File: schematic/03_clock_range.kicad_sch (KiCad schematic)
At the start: 23 parts, among them SW113 start / stop, SW114 octaves: stop at 3, U101 TLC555IDR, U102 TLC555IDR, U403 74HC14

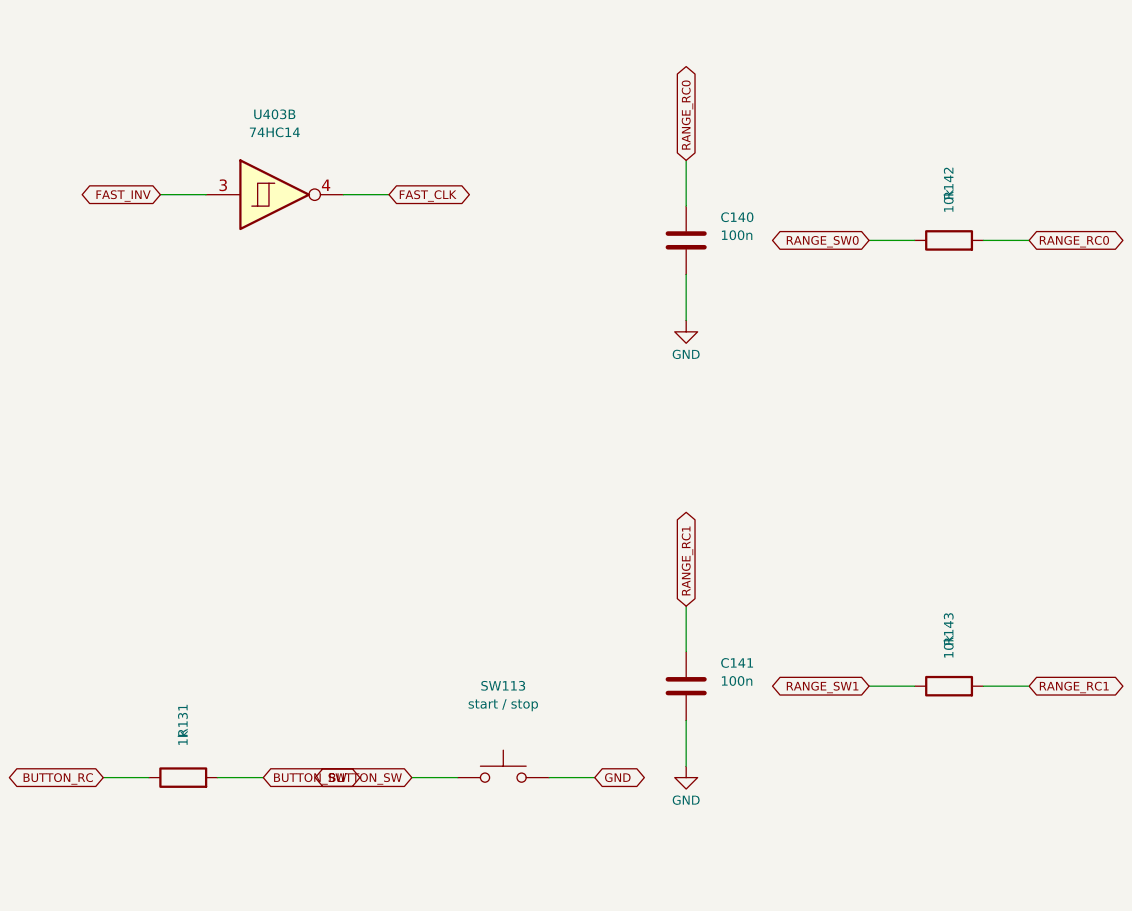
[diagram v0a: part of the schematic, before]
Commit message: add the pitch and sound circuit
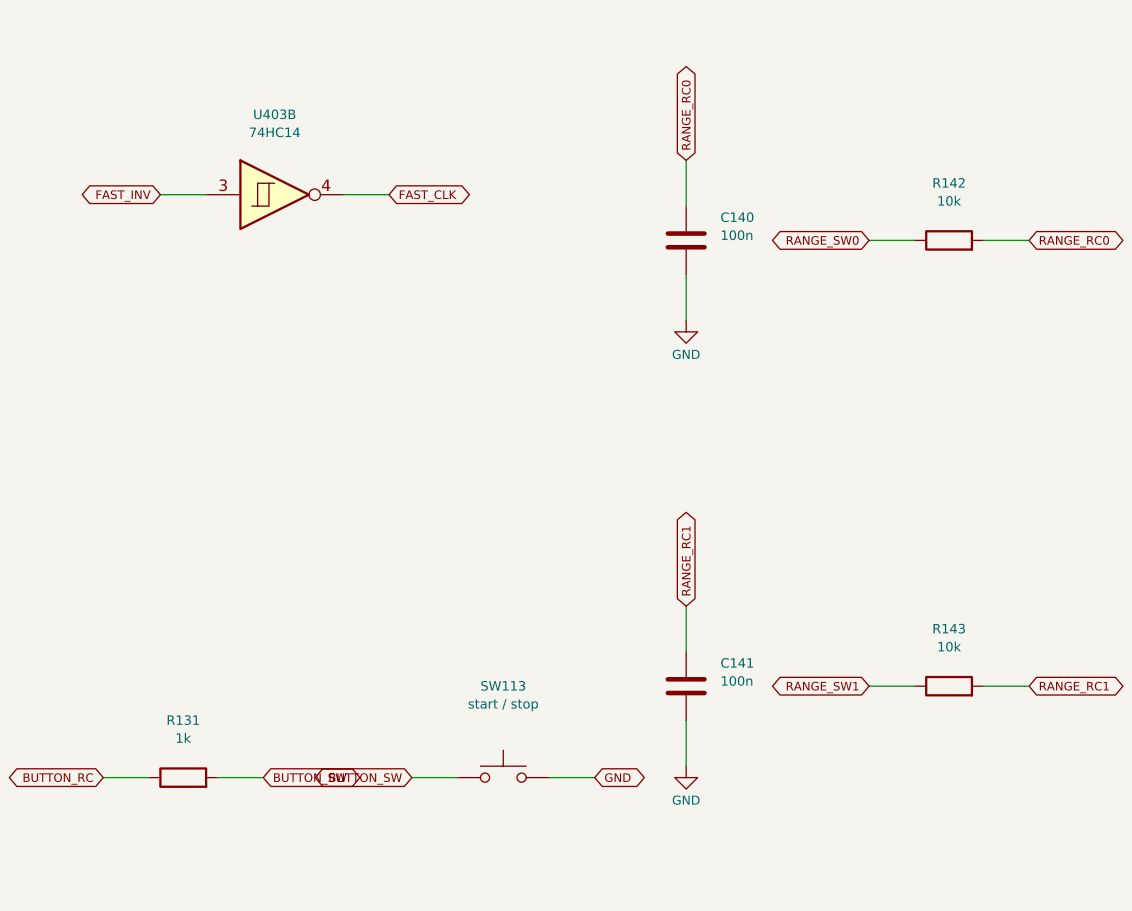
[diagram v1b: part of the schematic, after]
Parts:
- C181: footprint Capacitor_SMD:C_0805_2012Metric -> (none)
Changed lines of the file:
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@@
       )
     )
-    (property "Footprint" "Capacitor_SMD:C_0805_2012Metric"
+    (property "Footprint" ""
       (at 308.61 97.78999999999999 0.0)
       (effects
@@
     (dnp no)
     (property "Reference" "R131"
-      (at 119.38 223.52 0.0)
+      (at 119.38 223.52 90.0)
       (effects
         (font
@@
     )
     (property "Value" "1k"
-      (at 119.38 225.52 0.0)
+      (at 119.38 225.52 90.0)
       (effects
         (font
@@
     )
     (property "Footprint" "Resistor_SMD:R_0805_2012Metric"
-      (at 119.38 223.52 0.0)
+      (at 119.38 223.52 90.0)
       (effects
         (font
@@
     )
     (property "Datasheet" ""
-      (at 119.38 223.52 0.0)
+      (at 119.38 223.52 90.0)
       (effects
         (font
@@
     (dnp no)
     (property "Reference" "R142"
-      (at 204.47 163.83 0.0)
+      (at 204.47 163.83 90.0)
       (effects
         (font
@@
     )
     (property "Value" "10k"
-      (at 204.47 165.83 0.0)
+      (at 204.47 165.83 90.0)
       (effects
         (font
@@
     )
     (property "Footprint" "Resistor_SMD:R_0805_2012Metric"
-      (at 204.47 163.83 0.0)
+      (at 204.47 163.83 90.0)
       (effects
         (font
@@
     )
     (property "Datasheet" ""
-      (at 204.47 163.83 0.0)
+      (at 204.47 163.83 90.0)
       (effects
         (font
@@
     (dnp no)
     (property "Reference" "R143"
-      (at 204.47 213.36 0.0)
+      (at 204.47 213.36 90.0)
       (effects
         (font
@@
     )
     (property "Value" "10k"
-      (at 204.47 215.36 0.0)
+      (at 204.47 215.36 90.0)
       (effects
         (font
@@
     )
     (property "Footprint" "Resistor_SMD:R_0805_2012Metric"
-      (at 204.47 213.36 0.0)
+      (at 204.47 213.36 90.0)
       (effects
         (font
@@
     )
     (property "Datasheet" ""
-      (at 204.47 213.36 0.0)
-      (effects
-        (font
+      (at 204.47 213.36 90.0)
+      (effects
+        (font

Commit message: add power supply, rail checks and parts list
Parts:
- U101, U102: MPN (none) -> TLC555IDR; Manufacturer (none) -> Texas Instruments; Supplier (none) -> LCSC
- U403: MPN (none) -> 74HC14D,653; Manufacturer (none) -> Nexperia; Supplier (none) -> LCSC
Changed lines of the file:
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@@
       )
     )
-    (property "Datasheet" "http://www.ti.com/lit/ds/symlink/tlc555.pdf"
+    (property "Datasheet" "https://www.ti.com/lit/ds/symlink/tlc555.pdf"
       (at 62.230000000000004 57.15000000000001 0.0)
       (effects
@@
       )
     )
+    (property "MPN" "TLC555IDR"
+      (at 80.01 74.93 0.0)
+      (effects
+        (font
+          (size 1.0 1.0)
+        )
+        (hide yes)
+      )
+    )
+    (property "Manufacturer" "Texas Instruments"
+      (at 80.01 74.93 0.0)
+      (effects
+        (font
+          (size 1.0 1.0)
+        )
+        (hide yes)
+      )
+    )
+    (property "Supplier" "LCSC"
+      (at 80.01 74.93 0.0)
+      (effects
+        (font
+          (size 1.0 1.0)
+        )
+        (hide yes)
+      )
+    )
     (instances
       (project "arpeggiator"
@@
       )
     )
-    (property "Datasheet" "http://www.ti.com/lit/ds/symlink/tlc555.pdf"
+    (property "Datasheet" "https://www.ti.com/lit/ds/symlink/tlc555.pdf"
       (at 247.65 57.15000000000001 0.0)
       (effects
@@
       )
     )
+    (property "MPN" "TLC555IDR"
+      (at 265.43 74.93 0.0)
+      (effects
+        (font
+          (size 1.0 1.0)
+        )
+        (hide yes)
+      )
+    )
+    (property "Manufacturer" "Texas Instruments"
+      (at 265.43 74.93 0.0)
+      (effects
+        (font
+          (size 1.0 1.0)
+        )
+        (hide yes)
+      )
+    )
+    (property "Supplier" "LCSC"
+      (at 265.43 74.93 0.0)
+      (effects
+        (font
+          (size 1.0 1.0)
+        )
+        (hide yes)
+      )
+    )
     (instances
       (project "arpeggiator"
@@
       )
     )
-    (property "Datasheet" "http://www.ti.com/lit/gpn/sn74HC14"
+    (property "Datasheet" "https://assets.nexperia.com/documents/data-sheet/74HC_HCT14.pdf"
       (at 69.85 156.20999999999998 0.0)
       (effects
@@
       )
     )
+    (property "MPN" "74HC14D,653"
+      (at 69.85 165.1 0.0)
+      (effects
+        (font
+          (size 1.0 1.0)
+        )
+        (hide yes)
+      )
+    )
+    (property "Manufacturer" "Nexperia"
+      (at 69.85 165.1 0.0)
+      (effects
+        (font
+          (size 1.0 1.0)
+        )
+        (hide yes)
+      )
+    )
+    (property "Supplier" "LCSC"
+      (at 69.85 165.1 0.0)
+      (effects
+        (font
+          (size 1.0 1.0)
+        )
+        (hide yes)
+      )
+    )
     (instances
       (project "arpeggiator"
@@
       )
     )
-    (property "Datasheet" "http://www.ti.com/lit/gpn/sn74HC14"
+    (property "Datasheet" "https://assets.nexperia.com/documents/data-sheet/74HC_HCT14.pdf"
       (at 129.54 156.20999999999998 0.0)
       (effects
@@
       )
     )
+    (property "MPN" "74HC14D,653"
+      (at 129.54 165.1 0.0)
+      (effects
+        (font
+          (size 1.0 1.0)
+        )
+        (hide yes)
+      )
+    )
+    (property "Manufacturer" "Nexperia"
+      (at 129.54 165.1 0.0)
+      (effects
+        (font
+          (size 1.0 1.0)
+        )
+        (hide yes)
+      )
+    )
+    (property "Supplier" "LCSC"
+      (at 129.54 165.1 0.0)
+      (effects
+        (font
+          (size 1.0 1.0)
+        )
+        (hide yes)
+      )
+    )
     (instances
       (project "arpeggiator"
@@
       )
     )
-    (property "Datasheet" "http://www.ti.com/lit/gpn/sn74HC14"
+    (property "Datasheet" "https://assets.nexperia.com/documents/data-sheet/74HC_HCT14.pdf"
       (at 234.95 241.3 0.0)
       (effects
@@
         )
         (hide yes)
+      )
+    )
+    (property "MPN" "74HC14D,653"
+      (at 234.95 250.19 0.0)
+      (effects
+        (font
+          (size 1.0 1.0)
+        )
+        (hide yes)
+      )
+    )
+    (property "Manufacturer" "Nexperia"
+      (at 234.95 250.19 0.0)
+      (effects
+        (font
+          (size 1.0 1.0)
+        )
+        (hide yes)
+      )
+    )
+    (property "Supplier" "LCSC"
+      (at 234.95 250.19 0.0)
+      (effects
+        (font
+          (size 1.0 1.0)
+        )
+        (hide yes)

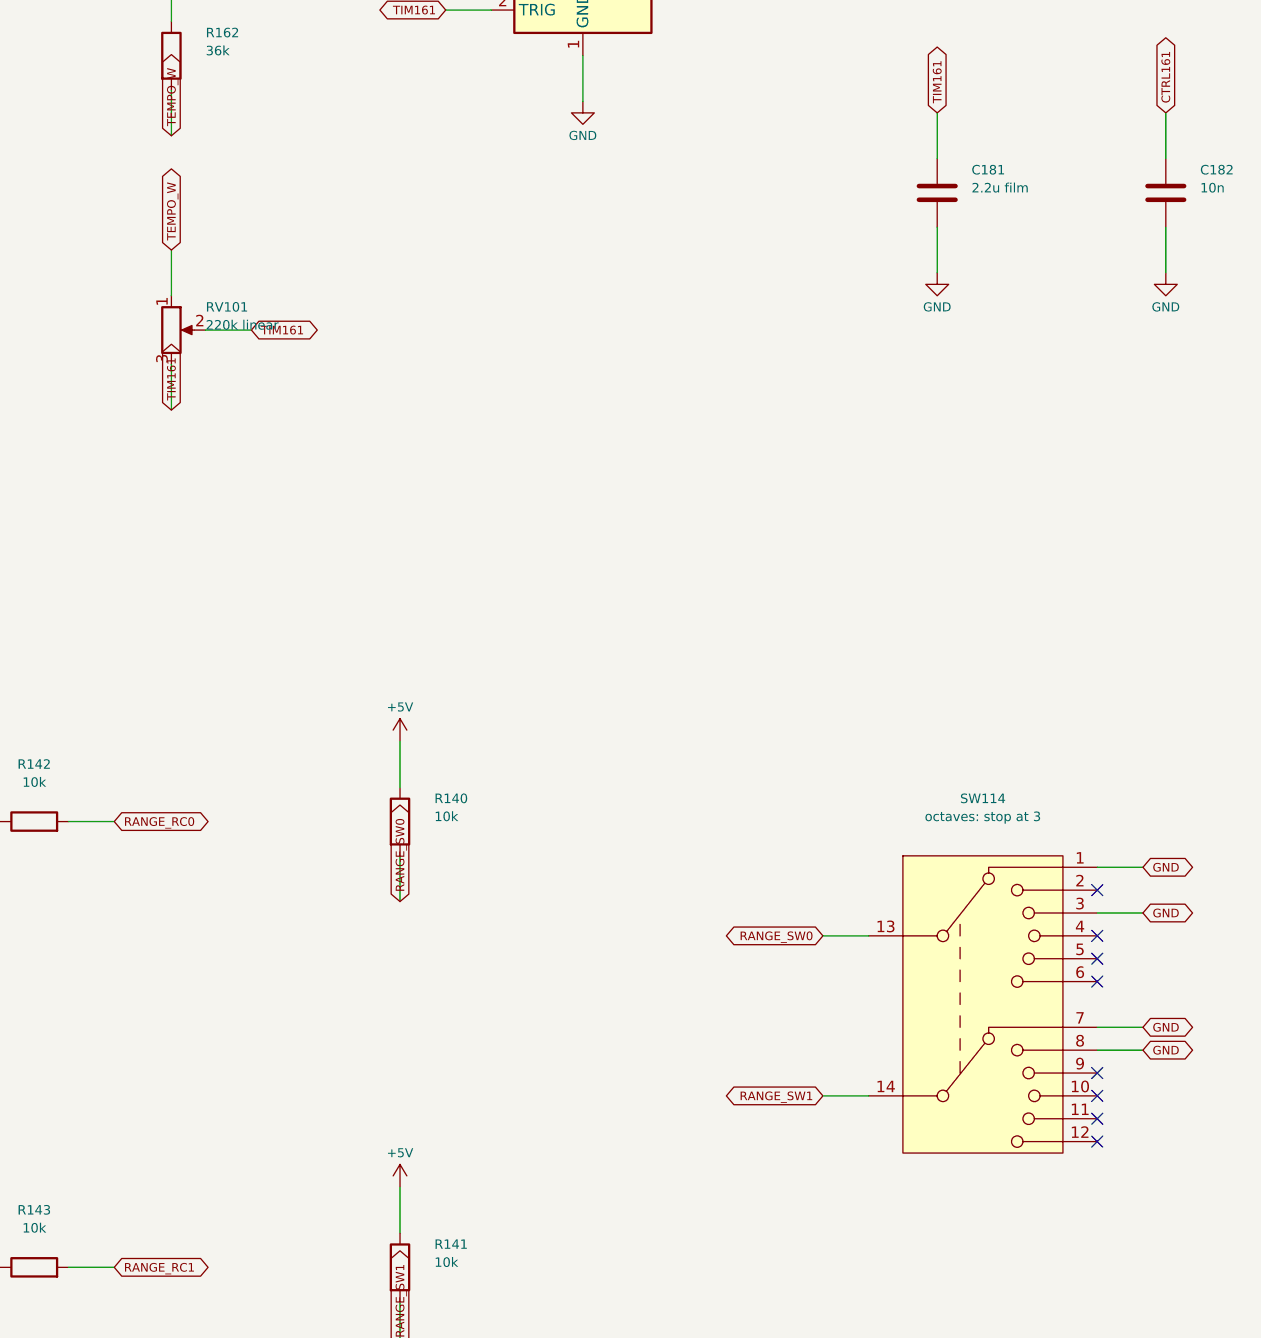
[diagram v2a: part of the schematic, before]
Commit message: pick controls and start pcb placement
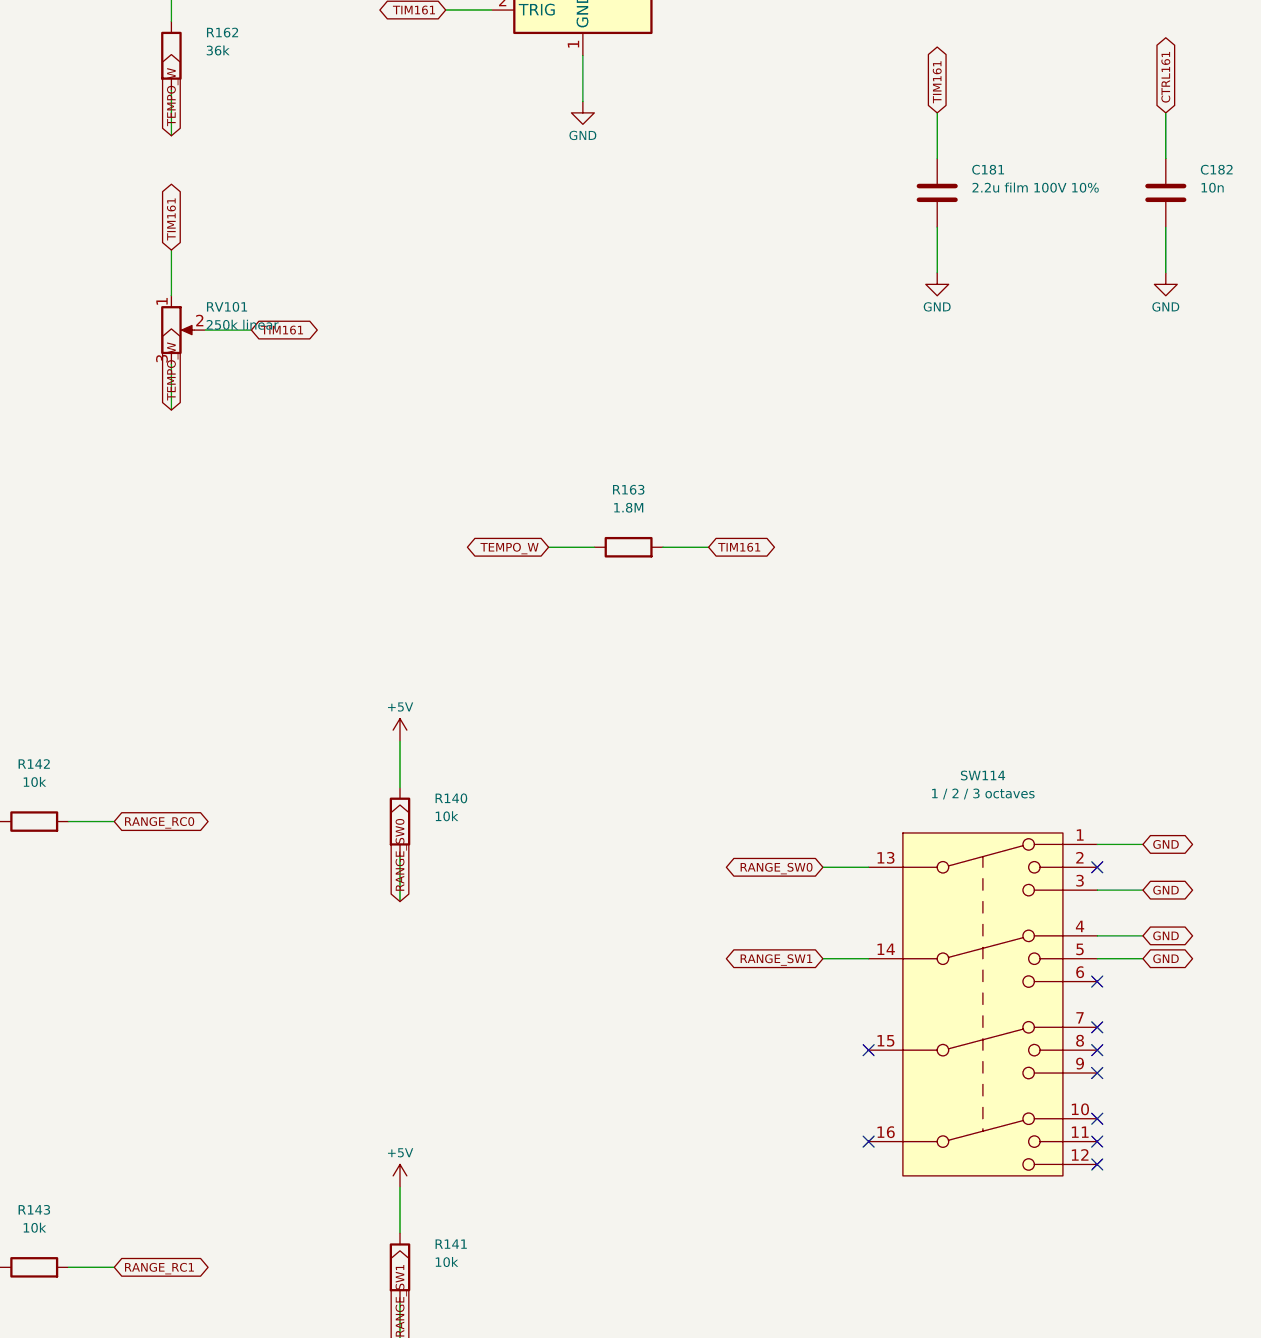
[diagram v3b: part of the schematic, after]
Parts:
- added R163: 1.8M, Resistor_SMD:R_0805_2012Metric, symbol Device:R
- C181: value 2.2u film -> 2.2u film 100V 10%; footprint (none) -> Capacitor_THT:C_Rect_L18.0mm_W8.0mm_P15.00mm_FKS3_FKP3; MPN (none) -> MKS4D042204F00KSSD; Manufacturer (none) -> WIMA; Supplier (none) -> Tayda; Supplier URL (none) -> https://www.taydaelectronics.com/capacitors/polyester-film-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
- RV101: value 220k linear -> 250k linear; footprint (none) -> Potentiometer_THT:Potentiometer_Alpha_RD901F-40-00D_Single_Vertical; MPN (none) -> RD901F-40-15F-B250K; Manufacturer (none) -> Taiwan Alpha; Supplier (none) -> Tayda; Supplier URL (none) -> https://www.taydaelectronics.com/potentiometer-variable-res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
- SW113: footprint (none) -> Button_Switch_THT:SW_SPST_Omron_B3F-40xx; MPN (none) -> B3F-4055; Manufacturer (none) -> Omron; Supplier (none) -> LCSC; Supplier URL (none) -> https://www.lcsc.com/product-detail/C84931.html
- SW114: value octaves: stop at 3 -> 1 / 2 / 3 octaves; footprint (none) -> Arpeggiator:SW_Alpha_SR2612F_4P3T; symbol Switch:SW_Rotary_2x6 -> Switch:SW_Rotary_4x3; MPN (none) -> SR2612F-0403-18R0B-D8-N; Manufacturer (none) -> Taiwan Alpha; Supplier (none) -> Tayda; Supplier URL (none) -> https://www.taydaelectronics.com/electromechanical/switches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
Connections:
- net GND: now also SW114.4, SW114.5; no longer SW114.7, SW114.8
- net TEMPO_W: now also RV101.3, R163.1; no longer RV101.1
- net TIM161: now also RV101.1, R163.2; no longer RV101.3
- no-connect marks 8 -> 10
